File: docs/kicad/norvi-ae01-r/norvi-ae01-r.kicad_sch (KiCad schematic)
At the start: 6 parts, among them U1 NORVI AE01-R, U2 DS18B20 Solar, U3 DS18B20 Pool

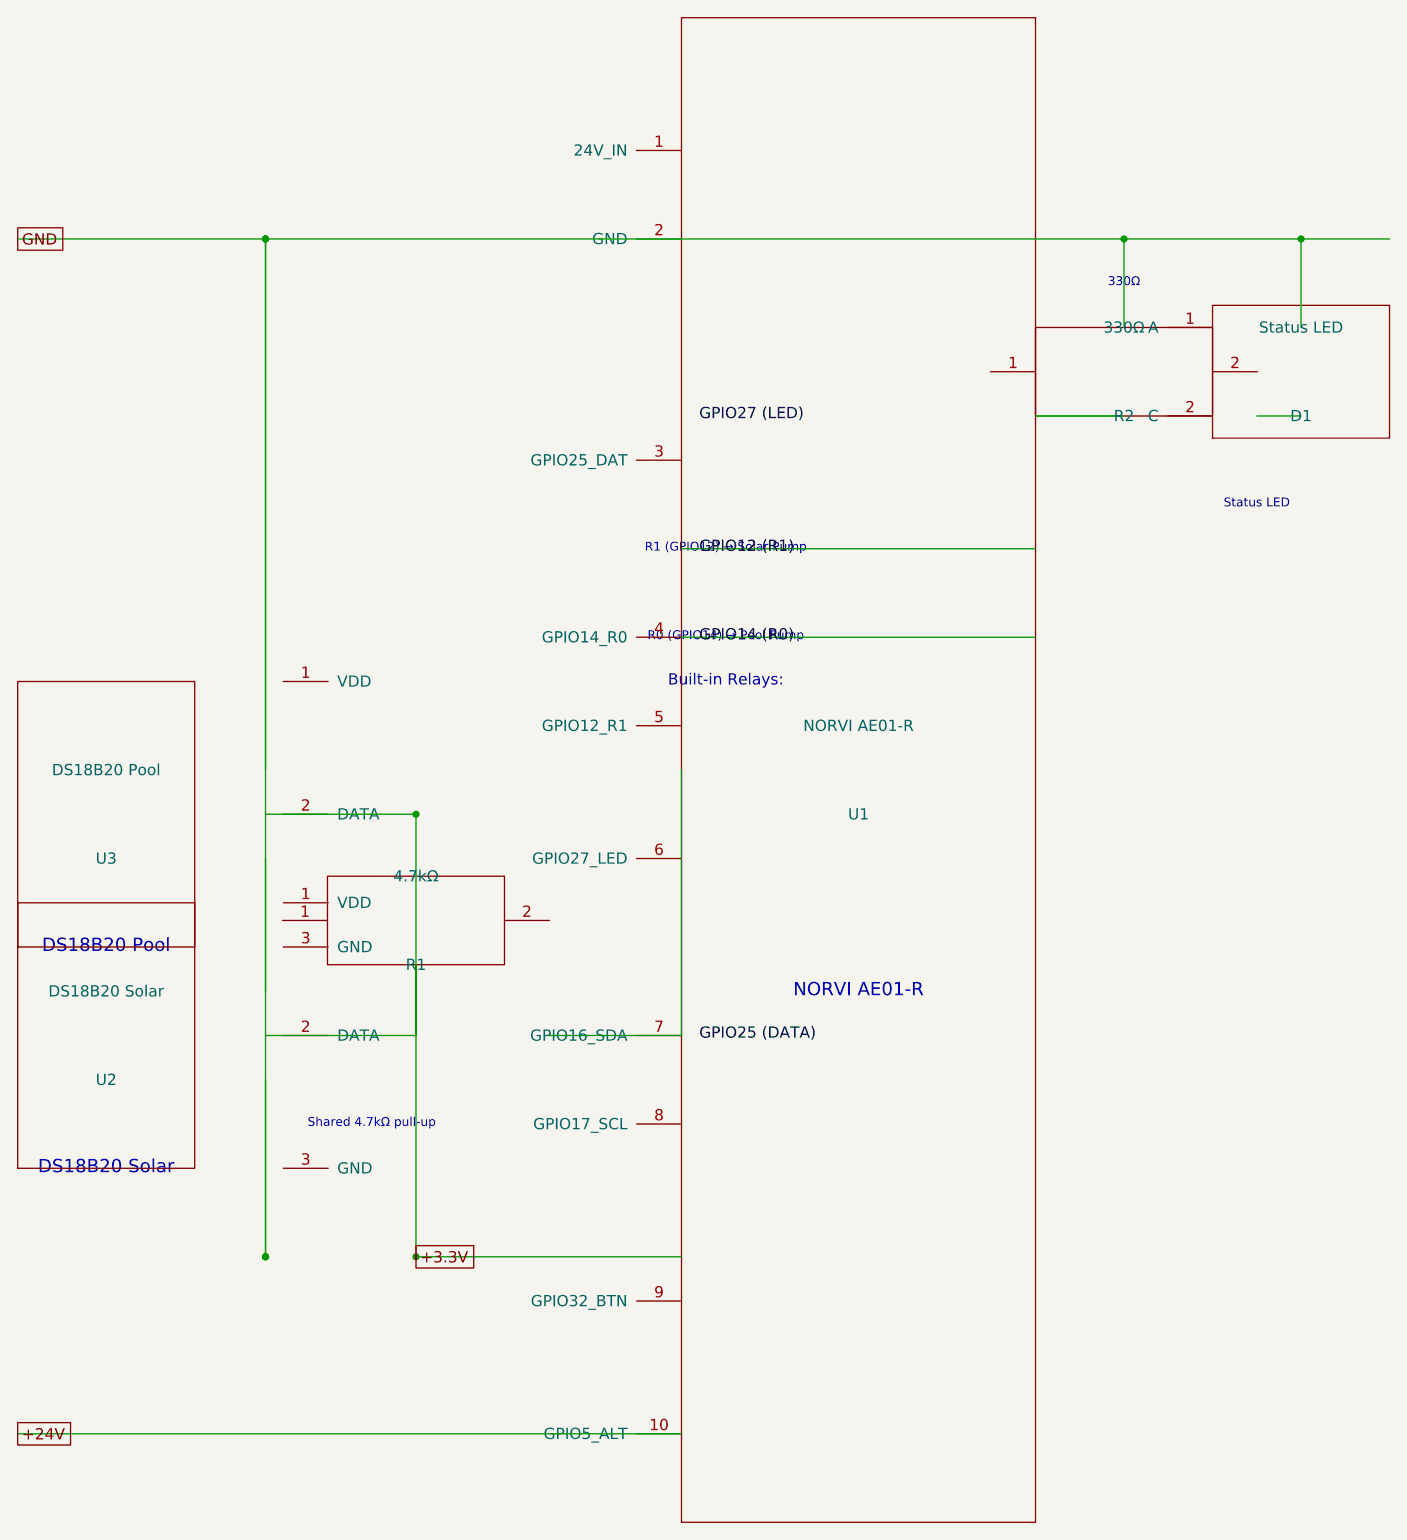
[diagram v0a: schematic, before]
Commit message: fix(docs): align KiCad schematic wires with pin coordinates after Y-axis inversion
- Add pin_tip() helper to convert local pin coordinates to absolute
  schematic positions with KiCad's Y-axis inversion
- Break power rails at each connection point so wire endpoints align
  with pin tips (fixes pin_not_connected ERC errors)
- Fix labels to match correct pin positions
- Add scripts/requirements.txt with sexpdata dependency (P2 review)
- Regenerate both variants, all remaining ERC violations are expected
  unused pins (GPIO2_LED, relay COM/NO terminals, NORVI spare GPIOs)

Fixes review P1: wire alignment with KiCad pin coordinates
Fixes review P2: sexpdata dependency declaration
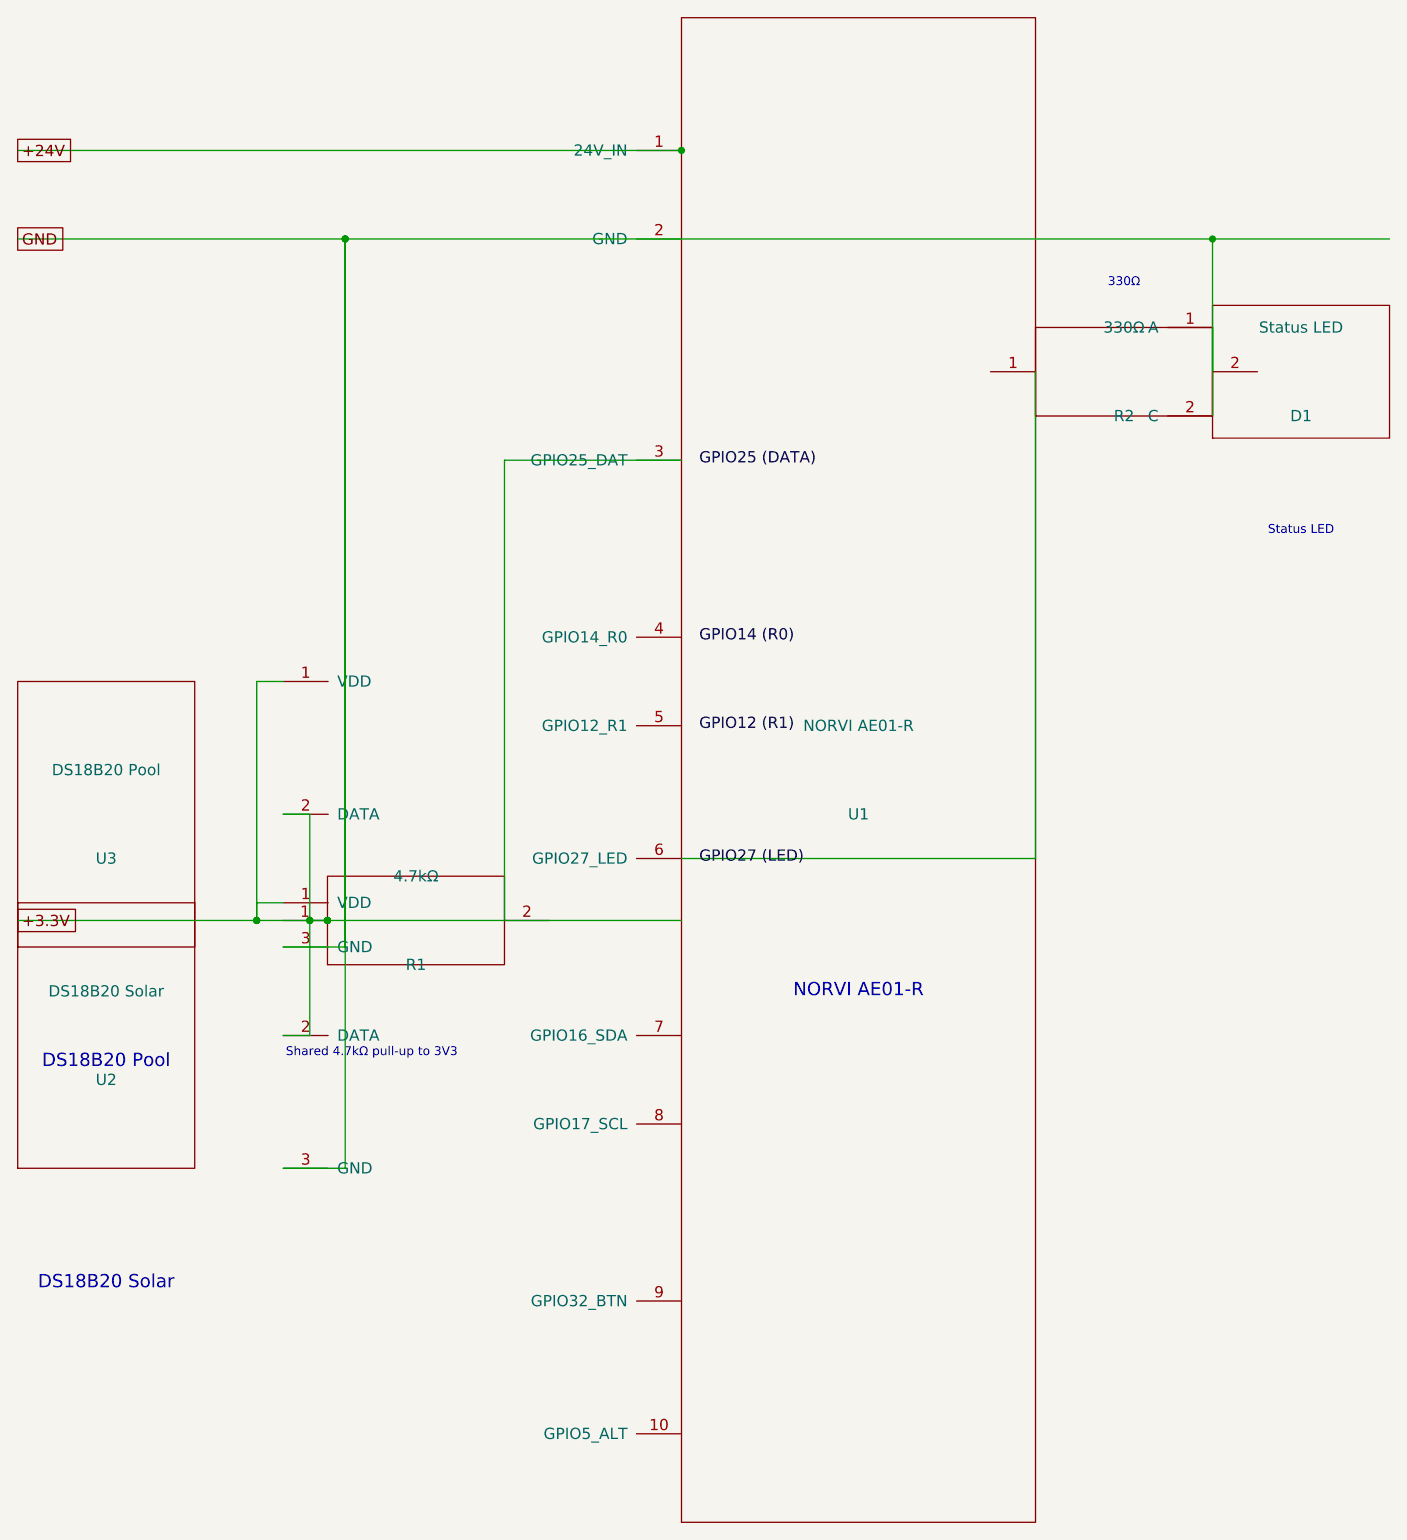
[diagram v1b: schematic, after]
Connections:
- net +24V: now also U1.1 (24V_IN); no longer U1.10 (GPIO5_ALT)
- net +3.3V: now also R1.1, U2.1 (VDD), U2.2 (DATA), U3.1 (VDD), U3.2 (DATA)
- net GND: now also D1.1 (A), D1.2 (C), R2.2, U1.2 (GND), U2.3 (GND), U3.3 (GND)
- net GPIO14 (R0): no longer U1.4 (GPIO14_R0)
- net GPIO27 (LED): now also R2.1, U1.6 (GPIO27_LED)
- net at U1.3 (GPIO25_DAT): now also R1.2
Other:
- note added: "Shared 4.7kΩ pull-up to 3V3"
- note removed: "Built-in Relays:"
- note removed: "R0 (GPIO14) → Pool Pump"
- note removed: "R1 (GPIO12) → Solar Pump"
- note removed: "Shared 4.7kΩ pull-up"
